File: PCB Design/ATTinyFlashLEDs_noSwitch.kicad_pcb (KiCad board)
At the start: 2 copper layers, 50 x 52.5 mm, 12 parts, among them J1 Conn_01x04_Pin, J2 Conn_01x04_Pin, J3 Conn_01x03_Pin, U1 ATtiny85V-10P

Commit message: Updates with front pour and stitching vias
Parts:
- moved J2 1.55 mm to (139.7, 86.1)
- moved J1 0.85 mm to (98.6, 86.1)
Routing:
- net Net-(J2-Pin_1): track 52.0 -> 75.9 mm, vias 1 -> 0
- net GND: track 18.1 -> 0.55 mm
- net Net-(D2-A): track 33.3 -> 29.7 mm
- net Net-(J2-Pin_4): track 18.0 -> 16.7 mm
- net Net-(D1-A): track 42.2 -> 40.9 mm
- added copper zone on F.Cu, net GND
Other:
- board size 50 x 52.5 mm -> 50 x 52.6 mm
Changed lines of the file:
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@@
 	(footprint "Connector_PinHeader_2.54mm:PinHeader_1x04_P2.54mm_Vertical"
 		(layer "F.Cu")
-		(at 97.79 85.725)
+		(at 98.552 86.106)
 		(descr "Through hole straight pin header, 1x04, 2.54mm pitch, single row")
 		(tags "Through hole pin header THT 1x04 2.54mm single row")
@@
 	(footprint "Connector_PinHeader_2.54mm:PinHeader_1x04_P2.54mm_Vertical"
 		(layer "F.Cu")
-		(at 141.224 85.862)
+		(at 139.7 86.116)
 		(descr "Through hole straight pin header, 1x04, 2.54mm pitch, single row")
 		(tags "Through hole pin header THT 1x04 2.54mm single row")
@@
 	)
 	(gr_rect
-		(start 94.996 67.388)
-		(end 144.996 119.888)
+		(start 94.996 67.31)
+		(end 145.034 119.888)
 		(stroke
 			(width 0.05)
@@
 	)
 	(segment
-		(start 141.224 90.942)
-		(end 123.581 90.942)
+		(start 123.327 91.196)
+		(end 139.7 91.196)
 		(width 0.254)
 		(layer "F.Cu")
@@
 	)
 	(segment
-		(start 141.224 88.402)
-		(end 123.581 88.402)
+		(start 130.927 88.656)
+		(end 135.509 84.074)
+		(width 0.254)
+		(layer "F.Cu")
+		(net 4)
+	)
+	(segment
+		(start 123.327 88.656)
+		(end 130.927 88.656)
 		(width 0.254)
 		(layer "F.Cu")
@@
 	)
 	(segment
-		(start 115.707 93.736)
-		(end 98.181 93.736)
+		(start 115.707 88.656)
+		(end 98.562 88.656)
 		(width 0.254)
 		(layer "F.Cu")
-		(net 5)
+		(net 6)
 	)
 	(segment
-		(start 115.707 88.656)
-		(end 98.181 88.656)
+		(start 98.562 88.656)
+		(end 98.552 88.646)
 		(width 0.254)
 		(layer "F.Cu")
@@
 	)
 	(segment
+		(start 113.528 91.196)
+		(end 113.518 91.186)
+		(width 0.254)
+		(layer "F.Cu")
+		(net 7)
+	)
+	(segment
 		(start 115.707 91.196)
-		(end 98.181 91.196)
+		(end 113.528 91.196)
+		(width 0.254)
+		(layer "F.Cu")
+		(net 7)
+	)
+	(segment
+		(start 113.518 91.186)
+		(end 98.552 91.186)
 		(width 0.254)
 		(layer "F.Cu")
@@
 	(segment
 		(start 115.707 86.116)
-		(end 98.181 86.116)
+		(end 98.562 86.116)
+		(width 0.254)
+		(layer "F.Cu")
+		(net 8)
+	)
+	(segment
+		(start 98.562 86.116)
+		(end 98.552 86.106)
 		(width 0.254)
 		(layer "F.Cu")
@@
 	)
 	(segment
-		(start 141.224 93.482)
-		(end 123.581 93.482)
+		(start 123.327 93.736)
+		(end 139.7 93.736)
 		(width 0.254)
 		(layer "F.Cu")
@@
 	)
 	(segment
-		(start 123.444 84.074)
-		(end 123.444 85.999)
+		(start 142.748 86.106)
+		(end 141.986 86.106)
+		(width 1.27)
+		(layer "F.Cu")
+		(net 11)
+	)
+	(segment
+		(start 123.327 69.205)
+		(end 123.327 86.116)
 		(width 1.27)
 		(layer "F.Cu")
@@
 	)
 	(segment
-		(start 141.224 85.862)
-		(end 123.581 85.862)
-		(width 0.254)
+		(start 123.444 69.088)
+		(end 123.327 69.205)
+		(width 1.27)
+		(layer "F.Cu")
+		(net 11)
+	)
+	(segment
+		(start 141.976 86.116)
+		(end 139.7 86.116)
+		(width 1.27)
 		(layer "F.Cu")
 		(net 11)
@@
 		(net 11)
 	)
-	(via
-		(at 123.444 84.074)
-		(size 0.6)
-		(drill 0.3)
-		(layers "F.Cu" "B.Cu")
-		(net 11)
-	)
 	(segment
-		(start 130.365 84.138)
-		(end 130.429 84.074)
+		(start 142.748 102.885)
+		(end 142.748 86.106)
 		(width 1.27)
-		(layer "B.Cu")
+		(layer "F.Cu")
 		(net 11)
 	)
 	(segment
 		(start 141.224 104.409)
-		(end 141.224 101.346)
+		(end 142.748 102.885)
 		(width 1.27)
-		(layer "B.Cu")
+		(layer "F.Cu")
 		(net 11)
 	)
 	(segment
-		(start 141.224 101.346)
-		(end 130.429 90.551)
+		(start 141.986 86.106)
+		(end 141.976 86.116)
 		(width 1.27)
-		(layer "B.Cu")
+		(layer "F.Cu")
 		(net 11)
 	)
 	(segment
-		(start 130.429 90.551)
-		(end 130.429 84.074)
+		(start 142.748 69.088)
+		(end 123.444 69.088)
 		(width 1.27)
-		(layer "B.Cu")
+		(layer "F.Cu")
 		(net 11)
 	)
 	(segment
-		(start 130.429 84.074)
-		(end 123.444 84.074)
+		(start 142.748 86.106)
+		(end 142.748 69.088)
 		(width 1.27)
-		(layer "B.Cu")
+		(layer "F.Cu")
 		(net 11)
 	)
 	(zone
+		(net 5)
+		(net_name "GND")
+		(layer "F.Cu")
+		(hatch edge 0.5)
+		(priority 1)
+		(connect_pads
+			(clearance 0.5)
+		)
+		(min_thickness 0.25)
+		(filled_areas_thickness no)
+		(fill yes
+			(thermal_gap 0.5)
+			(thermal_bridge_width 0.5)
+		)
+		(polygon
+			(pts
+				(xy 94.996 119.888) (xy 145.034 119.888) (xy 145.034 67.31) (xy 94.996 67.31)
+			)
+		)
+	)
+	(zone

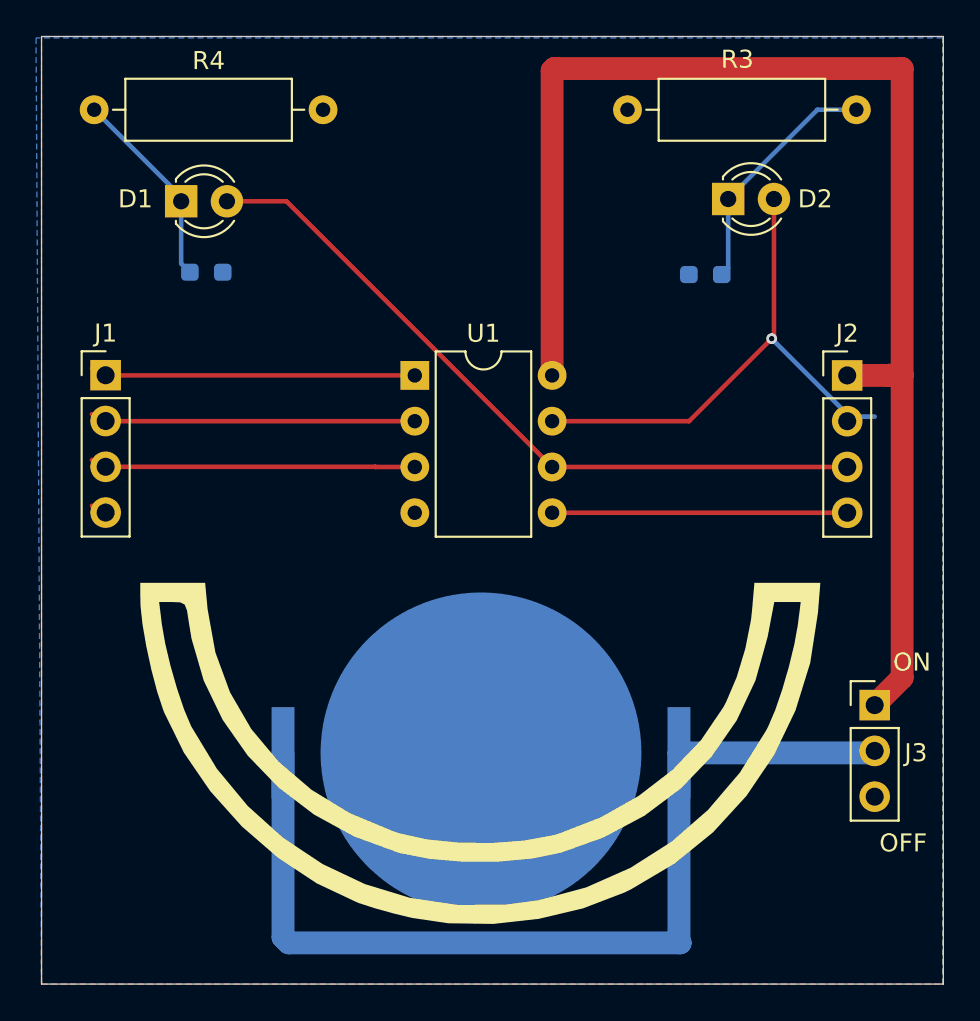
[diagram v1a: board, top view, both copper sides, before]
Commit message: Added decoupling capacitor, moved power trace to back copper
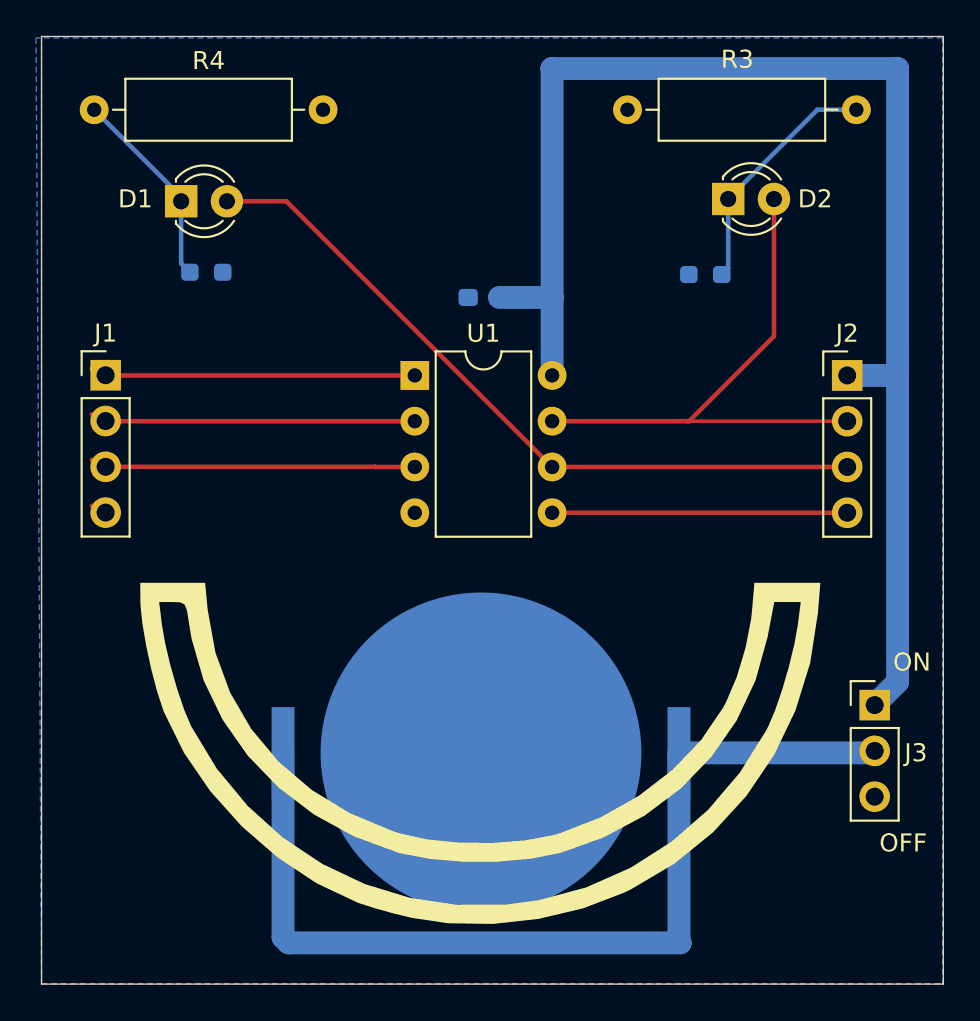
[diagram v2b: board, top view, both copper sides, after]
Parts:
- added C1: 0.1uF, Capacitor_SMD:C_0603_1608Metric_Pad1.08x0.95mm_HandSolder, B.Cu at (119.5, 81.8)
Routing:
- net Net-(J2-Pin_1): track 75.9 -> 78.3 mm
- net Net-(D2-A): track 29.7 -> 31.6 mm, vias 1 -> 0

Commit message: Updated pour and stitching vias
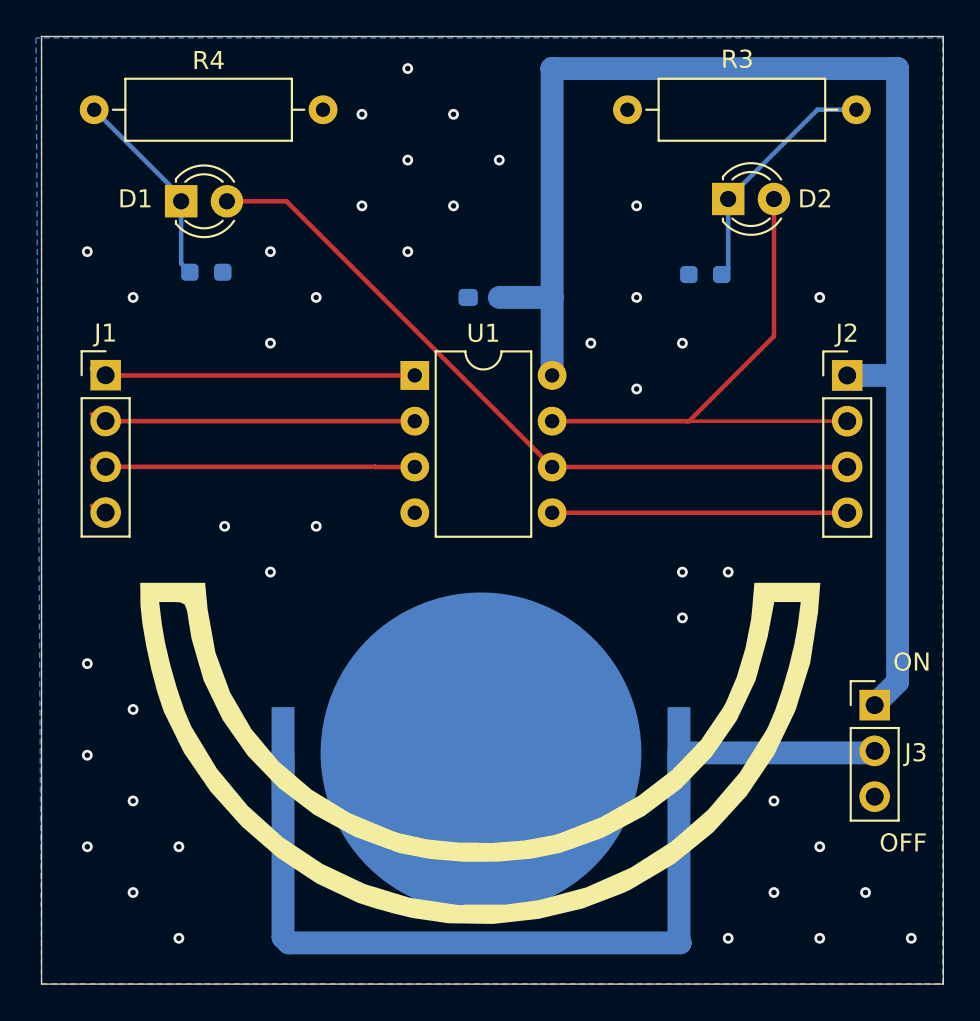
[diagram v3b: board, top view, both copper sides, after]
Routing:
- net GND: vias 0 -> 40
